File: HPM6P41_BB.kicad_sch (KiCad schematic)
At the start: 6 parts

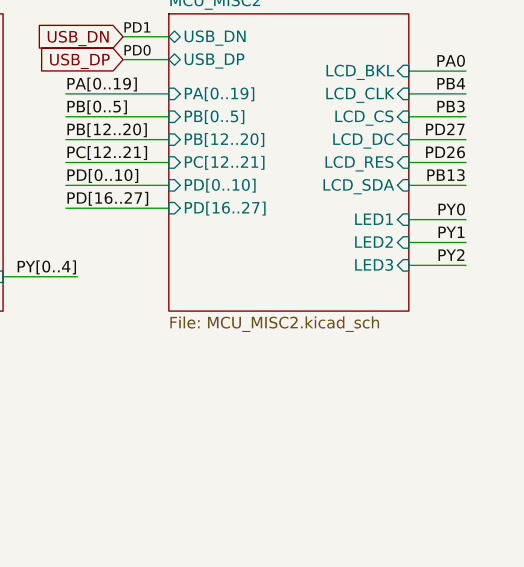
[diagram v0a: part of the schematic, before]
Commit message: 添加蜂鸣器IO及走线，更改PINMUX配图
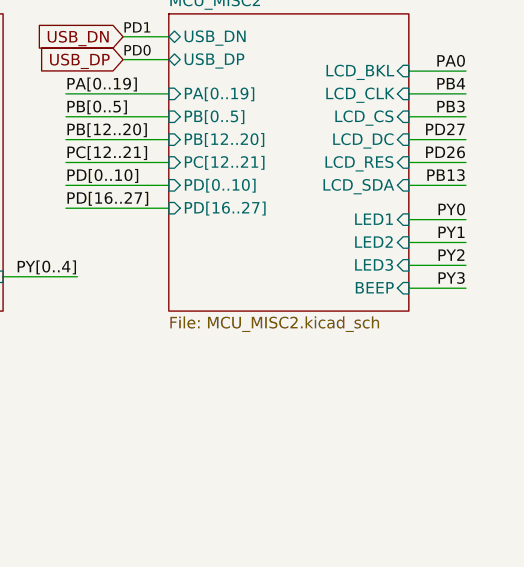
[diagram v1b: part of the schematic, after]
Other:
- sheet MCU_MISC2 ports: added BEEP; removed none
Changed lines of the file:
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@@
 	(wire
 		(pts
+			(xy 270.51 124.46) (xy 276.86 124.46)
+		)
+		(stroke
+			(width 0)
+			(type default)
+		)
+	)
+	(wire
+		(pts
 			(xy 201.93 66.04) (xy 196.85 66.04)
 		)
@@
 		)
 	)
+	(label "PY3"
+		(at 276.86 124.46 180)
+		(effects
+			(font
+				(size 1.27 1.27)
+			)
+			(justify right bottom)
+		)
+	)
 	(label "J_TDI"
 		(at 233.68 78.74 180)
@@
 			(effects
 				(font
+					(size 1.27 1.27)
+				)
+				(justify right)
+			)
+		)
+		(pin "BEEP" input
+			(at 270.51 124.46 0)
+			(effects
+				(font
